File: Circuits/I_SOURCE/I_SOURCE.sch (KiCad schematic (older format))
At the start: 29 parts, among them P1 +8, P2 -8, P3 GND, P4 OUTPUT, P5 I_SELECT, Q1 TIP127, U1 CA3140, U2 LM393

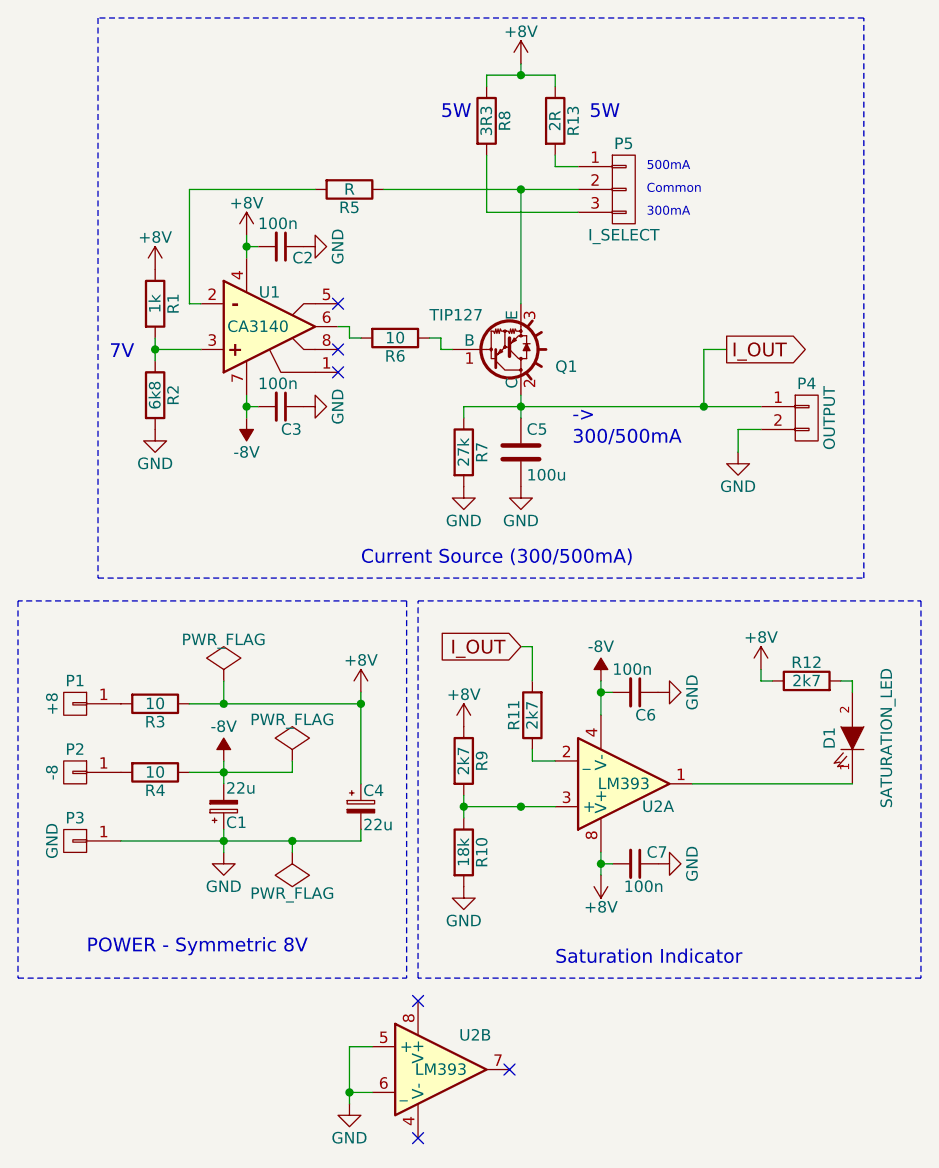
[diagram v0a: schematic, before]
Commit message: ADD: Current Source full PCB design
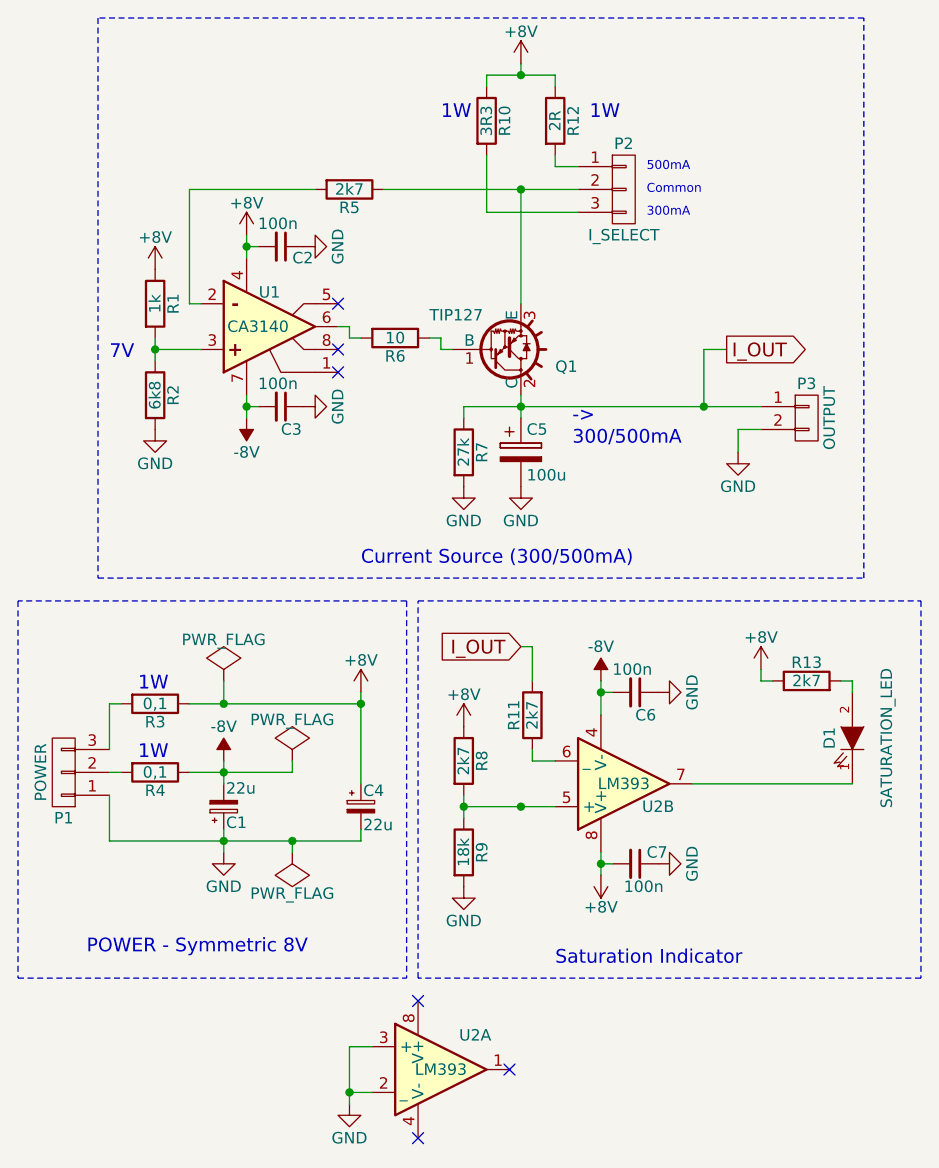
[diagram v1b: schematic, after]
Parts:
- removed C5: 100u, symbol C
- removed P1: +8, symbol CONN_01X01
- removed P2: -8, symbol CONN_01X01
- removed P3: GND, symbol CONN_01X01
- added C5: 100u, Capacitors_THT:CP_Radial_D6.3mm_P2.50mm, symbol CP
- added P1: POWER, Connectors:bornier3, symbol CONN_01X03
- C1, C4, C7: footprint (none) -> Capacitors_THT:CP_Radial_D5.0mm_P2.50mm
- C2, C3, C6: footprint (none) -> Capacitors_THT:C_Rect_L7.0mm_W2.5mm_P5.00mm
- D1: footprint (none) -> LEDs:LED_D5.0mm
- P2: renamed from P5; footprint (none) -> Pin_Headers:Pin_Header_Straight_1x03_Pitch2.00mm
- P3: renamed from P4; footprint (none) -> Connectors:bnc-ci
- Q1: footprint TO-220 -> Power_Integrations:TO-220
- R1, R11, R2, R6, R7: footprint (none) -> w_pth_resistors:RC03
- R10: renamed from R8; footprint (none) -> Resistors_THT:R_Axial_DIN0309_L9.0mm_D3.2mm_P12.70mm_Horizontal
- R12: renamed from R13; footprint (none) -> Resistors_THT:R_Axial_DIN0309_L9.0mm_D3.2mm_P12.70mm_Horizontal
- R13: renamed from R12; footprint (none) -> w_pth_resistors:RC03
- R3, R4: value 10 -> 0,1; footprint (none) -> Resistors_THT:R_Axial_DIN0309_L9.0mm_D3.2mm_P12.70mm_Horizontal
- R5: value R -> 2k7; footprint (none) -> w_pth_resistors:RC03
- R8: renamed from R9; footprint (none) -> w_pth_resistors:RC03
- R9: renamed from R10; footprint (none) -> w_pth_resistors:RC03
- U1, U2: footprint (none) -> Housings_DIP:DIP-8_W7.62mm_LongPads
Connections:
- net GND: now also U2.2 (_), U2.3 (+), C5.2, P1.1 (P1); no longer U2.5 (+), U2.6 (_)
- net I_OUT: now also C5.1
- net at D1.1 (K): now also U2.7; no longer U2.1
- net at R11.1: now also U2.6 (_); no longer U2.2 (_)
- net at R8.2, R9.1: now also U2.5 (+); no longer U2.3 (+)
- net at R3.2: now also P1.3 (P3)
- net at R4.2: now also P1.2 (P2)
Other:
- note added: "1W"
- note removed: "5W"
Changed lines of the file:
@@
 encoding utf-8
 Sheet 1 1
-Title "Current Source for Materials Analysis"
-Date "2017-12-15"
+Title "SADAMAP Current Source "
+Date "2018-01-31"
 Rev "1"
-Comp "LAPMA - UFRGS"
-Comment1 "All resistors are 1/8W, except R8"
+Comp "LAPMA/CTA - IF/UFRGS"
+Comment1 "All resistors are 1/4W, 1% precision, except R3, R4, R8 and R13. "
 Comment2 "300mA and 500mA Selectable DC Current Source"
 Comment3 "There's a saturation indicator for output higher than 7V"
@@
 F 0 "U1" H 1950 2100 50  0000 C CNN
 F 1 "CA3140" H 1900 2250 50  0000 C CNN
-F 2 "" H 1850 2150 50  0000 C CNN
+F 2 "Housings_DIP:DIP-8_W7.62mm_LongPads" H 1850 2150 50  0001 C CNN
 F 3 "" H 1950 2250 50  0000 C CNN
 	1    1950 2250
@@
 P 2300 1650
 F 0 "R5" V 2380 1650 50  0000 C CNN
-F 1 "R" V 2300 1650 50  0000 C CNN
-F 2 "" V 2230 1650 50  0000 C CNN
+F 1 "2k7" V 2300 1650 50  0000 C CNN
+F 2 "w_pth_resistors:RC03" V 2230 1650 50  0001 C CNN
 F 3 "" H 2300 1650 50  0000 C CNN
 	1    2300 1650
@@
 	1600 2150 1650 2150
 $Comp
-L R R8
+L R R10
 U 1 1 5A2F411C
 P 2900 1350
-F 0 "R8" V 2980 1350 50  0000 C CNN
+F 0 "R10" V 2980 1350 50  0000 C CNN
 F 1 "3R3" V 2900 1350 50  0000 C CNN
-F 2 "" V 2830 1350 50  0000 C CNN
+F 2 "Resistors_THT:R_Axial_DIN0309_L9.0mm_D3.2mm_P12.70mm_Horizontal" V 2830 1350 50  0001 C CNN
 F 3 "" H 2900 1350 50  0000 C CNN
 	1    2900 1350
@@
 F 0 "Q1" H 3200 2425 50  0000 L CNN
 F 1 "TIP127" H 2650 2200 50  0000 L CNN
-F 2 "TO-220" H 2600 2250 50  0001 L CIN
+F 2 "Power_Integrations:TO-220" H 2600 2250 50  0001 L CIN
 F 3 "" H 2950 2350 50  0000 L CNN
 	1    2950 2350
@@
 F 0 "R6" V 2580 2300 50  0000 C CNN
 F 1 "10" V 2500 2300 50  0000 C CNN
-F 2 "" V 2430 2300 50  0000 C CNN
+F 2 "w_pth_resistors:RC03" V 2430 2300 50  0001 C CNN
 F 3 "" H 2500 2300 50  0000 C CNN
 	1    2500 2300
@@
 F 0 "R7" V 2880 2800 50  0000 C CNN
 F 1 "27k" V 2800 2800 50  0000 C CNN
-F 2 "" V 2730 2800 50  0000 C CNN
+F 2 "w_pth_resistors:RC03" V 2730 2800 50  0001 C CNN
 F 3 "" H 2800 2800 50  0000 C CNN
 	1    2800 2800
-	1    0    0    -1
-$EndComp
-$Comp
-L C C5
-U 1 1 5A2F43CF
-P 3050 2800
-F 0 "C5" H 3075 2900 50  0000 L CNN
-F 1 "100u" H 3075 2700 50  0000 L CNN
-F 2 "" H 3088 2650 50  0000 C CNN
-F 3 "" H 3050 2800 50  0000 C CNN
-	1    3050 2800
 	1    0    0    -1
 $EndComp
@@
 $Comp
 L LM393 U2
-U 1 1 5A2F4B6B
+U 2 1 5A2F4B6B
 P 3500 4250
 F 0 "U2" H 3650 4350 50  0000 C CNN
 F 1 "LM393" H 3500 4250 50  0000 C CNN
-F 2 "" H 3500 4250 50  0000 C CNN
+F 2 "Housings_DIP:DIP-8_W7.62mm_LongPads" H 3500 4250 50  0001 C CNN
 F 3 "" H 3500 4250 50  0000 C CNN
-	1    3500 4250
+	2    3500 4250
 	1    0    0    1
 $EndComp
 $Comp
 L LM393 U2
-U 2 1 5A2F4B6C
+U 1 1 5A2F4B6C
 P 2700 5500
 F 0 "U2" H 2850 5650 50  0000 C CNN
 F 1 "LM393" H 2700 5500 50  0000 C CNN
-F 2 "" H 2700 5500 50  0000 C CNN
+F 2 "Housings_DIP:DIP-8_W7.62mm_LongPads" H 2700 5500 50  0001 C CNN
 F 3 "" H 2700 5500 50  0000 C CNN
-	2    2700 5500
+	1    2700 5500
 	1    0    0    -1
 $EndComp
@@
 F 0 "R11" V 3180 3950 50  0000 C CNN
 F 1 "2k7" V 3100 3950 50  0000 C CNN
-F 2 "" V 3030 3950 50  0000 C CNN
+F 2 "w_pth_resistors:RC03" V 3030 3950 50  0001 C CNN
 F 3 "" H 3100 3950 50  0000 C CNN
 	1    3100 3950
@@
 F 0 "C6" V 3650 3850 50  0000 L CNN
 F 1 "100n" V 3450 3750 50  0000 L CNN
-F 2 "" H 3550 3850 50  0000 C CNN
+F 2 "Capacitors_THT:C_Rect_L7.0mm_W2.5mm_P5.00mm" H 3550 3850 50  0001 C CNN
 F 3 "" H 3550 3850 50  0000 C CNN
 	1    3550 3850
@@
 $EndComp
 $Comp
-L R R9
+L R R8
 U 1 1 5A2F4B71
 P 2800 4150
-F 0 "R9" V 2880 4150 50  0000 C CNN
+F 0 "R8" V 2880 4150 50  0000 C CNN
 F 1 "2k7" V 2800 4150 50  0000 C CNN
-F 2 "" V 2730 4150 50  0000 C CNN
+F 2 "w_pth_resistors:RC03" V 2730 4150 50  0001 C CNN
 F 3 "" H 2800 4150 50  0000 C CNN
 	1    2800 4150
@@
 $EndComp
 $Comp
-L R R10
+L R R9
 U 1 1 5A2F4B72
 P 2800 4550
-F 0 "R10" V 2880 4550 50  0000 C CNN
+F 0 "R9" V 2880 4550 50  0000 C CNN
 F 1 "18k" V 2800 4550 50  0000 C CNN
-F 2 "" V 2730 4550 50  0000 C CNN
+F 2 "w_pth_resistors:RC03" V 2730 4550 50  0001 C CNN
 F 3 "" H 2800 4550 50  0000 C CNN
 	1    2800 4550
@@
 F 0 "C7" V 3600 4650 50  0000 L CNN
 F 1 "100n" V 3450 4550 50  0000 L CNN
-F 2 "" H 3550 4600 50  0000 C CNN
+F 2 "Capacitors_THT:CP_Radial_D5.0mm_P2.50mm" H 3550 4600 50  0001 C CNN
 F 3 "" H 3550 4600 50  0000 C CNN
 	1    3550 4600
@@
 F 0 "D1" H 4500 3950 50  0000 C CNN
 F 1 "SATURATION_LED" H 4500 4200 50  0000 C CNN
-F 2 "" H 4500 4050 50  0000 C CNN
+F 2 "LEDs:LED_D5.0mm" H 4500 4050 50  0001 C CNN
 F 3 "" H 4500 4050 50  0000 C CNN
 	1    4500 4050
@@
 $EndComp
 $Comp
-L R R12
+L R R13
 U 1 1 5A2F4B7B
 P 4300 3800
-F 0 "R12" V 4380 3800 50  0000 C CNN
+F 0 "R13" V 4380 3800 50  0000 C CNN
 F 1 "2k7" V 4300 3800 50  0000 C CNN
-F 2 "" V 4230 3800 50  0000 C CNN
+F 2 "w_pth_resistors:RC03" V 4230 3800 50  0001 C CNN
 F 3 "" H 4300 3800 50  0000 C CNN
 	1    4300 3800
@@
 NoConn ~ 3000 5500
 $Comp
-L CONN_01X01 P1
-U 1 1 5A2F4B7E
-P 1100 3900
-F 0 "P1" H 1100 4000 50  0000 C CNN
-F 1 "+8" V 1200 3900 50  0000 C CNN
-F 2 "" H 1100 3900 50  0000 C CNN
-F 3 "" H 1100 3900 50  0000 C CNN
-	1    1100 3900
-	-1   0    0    -1
-$EndComp
-$Comp
-L CONN_01X01 P2
-U 1 1 5A2F4B7F
-P 1100 4200
-F 0 "P2" H 1100 4300 50  0000 C CNN
-F 1 "-8" V 1200 4200 50  0000 C CNN
-F 2 "" H 1100 4200 50  0000 C CNN
-F 3 "" H 1100 4200 50  0000 C CNN
-	1    1100 4200
-	-1   0    0    -1
-$EndComp
-$Comp
-L CONN_01X01 P3
-U 1 1 5A2F4B80
-P 1100 4500
-F 0 "P3" H 1100 4600 50  0000 C CNN
-F 1 "GND" V 1200 4500 50  0000 C CNN
-F 2 "" H 1100 4500 50  0000 C CNN
-F 3 "" H 1100 4500 50  0000 C CNN
-	1    1100 4500
-	-1   0    0    -1
-$EndComp
-$Comp
 L R R3
 U 1 1 5A2F4B81
 P 1450 3900
 F 0 "R3" V 1530 3900 50  0000 C CNN
-F 1 "10" V 1450 3900 50  0000 C CNN
-F 2 "" V 1380 3900 50  0000 C CNN
+F 1 "0,1" V 1450 3900 50  0000 C CNN
+F 2 "Resistors_THT:R_Axial_DIN0309_L9.0mm_D3.2mm_P12.70mm_Horizontal" V 1380 3900 50  0001 C CNN
 F 3 "" H 1450 3900 50  0000 C CNN
 	1    1450 3900
@@
 P 1450 4200
 F 0 "R4" V 1530 4200 50  0000 C CNN
-F 1 "10" V 1450 4200 50  0000 C CNN
-F 2 "" V 1380 4200 50  0000 C CNN
+F 1 "0,1" V 1450 4200 50  0000 C CNN
+F 2 "Resistors_THT:R_Axial_DIN0309_L9.0mm_D3.2mm_P12.70mm_Horizontal" V 1380 4200 50  0001 C CNN
 F 3 "" H 1450 4200 50  0000 C CNN
 	1    1450 4200
@@
 F 0 "C1" H 1760 4420 50  0000 L CNN
 F 1 "22u" H 1760 4270 50  0000 L CNN
-F 2 "" H 1750 4350 50  0000 C CNN
+F 2 "Capacitors_THT:CP_Radial_D5.0mm_P2.50mm" H 1750 4350 50  0001 C CNN
 F 3 "" H 1750 4350 50  0000 C CNN
 	1    1750 4350
@@
 F 0 "C4" H 2360 4420 50  0000 L CNN
 F 1 "22u" H 2360 4270 50  0000 L CNN
-F 2 "" H 2350 4350 50  0000 C CNN
+F 2 "Capacitors_THT:CP_Radial_D5.0mm_P2.50mm" H 2350 4350 50  0001 C CNN
 F 3 "" H 2350 4350 50  0000 C CNN
 	1    2350 4350
@@
 	1750 4450 1750 4550
 Wire Wire Line
-	1300 4500 2350 4500
+	1250 4500 2350 4500
 Wire Wire Line
 	2350 4500 2350 4450
@@
 F 0 "R1" V 1530 2150 50  0000 C CNN
 F 1 "1k" V 1450 2150 50  0000 C CNN
-F 2 "" V 1380 2150 50  0000 C CNN
+F 2 "w_pth_resistors:RC03" V 1380 2150 50  0001 C CNN
 F 3 "" H 1450 2150 50  0000 C CNN
 	1    1450 2150
@@
 F 0 "R2" V 1530 2550 50  0000 C CNN
 F 1 "6k8" V 1450 2550 50  0000 C CNN
-F 2 "" V 1380 2550 50  0000 C CNN
+F 2 "w_pth_resistors:RC03" V 1380 2550 50  0001 C CNN
 F 3 "" H 1450 2550 50  0000 C CNN
 	1    1450 2550
@@
 F 0 "C3" V 2100 2600 50  0000 L CNN
 F 1 "100n" V 1900 2500 50  0000 L CNN
-F 2 "" H 2000 2600 50  0000 C CNN
+F 2 "Capacitors_THT:C_Rect_L7.0mm_W2.5mm_P5.00mm" H 2000 2600 50  0001 C CNN
 F 3 "" H 2000 2600 50  0000 C CNN
 	1    2000 2600
@@
 F 0 "C2" V 2050 1950 50  0000 L CNN
 F 1 "100n" V 1900 1800 50  0000 L CNN
-F 2 "" H 2000 1900 50  0000 C CNN
+F 2 "Capacitors_THT:C_Rect_L7.0mm_W2.5mm_P5.00mm" H 2000 1900 50  0001 C CNN
 F 3 "" H 2000 1900 50  0000 C CNN
 	1    2000 1900
@@
 	2800 2600 4100 2600
 $Comp
-L CONN_01X02 P4
+L CONN_01X02 P3
 U 1 1 5A2F6EE0
 P 4300 2650
-F 0 "P4" H 4300 2800 50  0000 C CNN
+F 0 "P3" H 4300 2800 50  0000 C CNN
 F 1 "OUTPUT" V 4400 2650 50  0000 C CNN
-F 2 "" H 4300 2650 50  0000 C CNN
+F 2 "Connectors:bnc-ci" H 4300 2650 50  0001 C CNN
 F 3 "" H 4300 2650 50  0000 C CNN
 	1    4300 2650
@@
 7V
 Text Notes 2700 1350 0    60   ~ 0
-5W
+1W
 Text Notes 2350 3300 0    60   ~ 0
 Current Source (300/500mA)
@@
 	2600 3450 4800 3450
 $Comp
-L R R13
+L R R12
 U 1 1 5A4CC621
 P 3200 1350
-F 0 "R13" V 3280 1350 50  0000 C CNN
+F 0 "R12" V 3280 1350 50  0000 C CNN
 F 1 "2R" V 3200 1350 50  0000 C CNN
-F 2 "" V 3130 1350 50  0000 C CNN
+F 2 "Resistors_THT:R_Axial_DIN0309_L9.0mm_D3.2mm_P12.70mm_Horizontal" V 3130 1350 50  0001 C CNN
 F 3 "" H 3200 1350 50  0000 C CNN
 	1    3200 1350
@@
 $EndComp
 Text Notes 3350 1350 0    60   ~ 0
-5W
+1W
 Wire Wire Line
 	2900 1200 2900 1150
@@
 Connection ~ 3050 1150
 $Comp
-L CONN_01X03 P5
+L CONN_01X03 P2
 U 1 1 5A4CD4EF
 P 3500 1650
-F 0 "P5" H 3500 1850 50  0000 C CNN
+F 0 "P2" H 3500 1850 50  0000 C CNN
 F 1 "I_SELECT" H 3500 1450 50  0000 C CNN
-F 2 "" H 3500 1650 50  0000 C CNN
+F 2 "Pin_Headers:Pin_Header_Straight_1x03_Pitch2.00mm" H 3500 1650 50  0001 C CNN
 F 3 "" H 3500 1650 50  0000 C CNN
 	1    3500 1650
@@
 Text Notes 3600 1675 0    39   ~ 0
 Common
+Text Notes 1375 3850 0    60   ~ 0
+1W
+Text Notes 1375 4150 0    60   ~ 0
+1W
+$Comp
+L CP C5
+U 1 1 5A724097
+P 3050 2800
+F 0 "C5" H 3075 2900 50  0000 L CNN
+F 1 "100u" H 3075 2700 50  0000 L CNN
+F 2 "Capacitors_THT:CP_Radial_D6.3mm_P2.50mm" H 3088 2650 50  0001 C CNN
+F 3 "" H 3050 2800 50  0000 C CNN
+	1    3050 2800
+	1    0    0    -1
+$EndComp
+$Comp
+L CONN_01X03 P1
+U 1 1 5A7244BA
+P 1050 4200
+F 0 "P1" H 1050 4400 50  0000 C CNN
+F 1 "POWER" V 1150 4200 50  0000 C CNN
+F 2 "Connectors:bornier3" H 1050 4200 50  0001 C CNN
+F 3 "" H 1050 4200 50  0000 C CNN
+	1    1050 4200
+	-1   0    0    1
+$EndComp
+Wire Wire Line
+	1250 4200 1300 4200
+Wire Wire Line
+	1250 4100 1250 3900
+Wire Wire Line
+	1250 3900 1300 3900
+Wire Wire Line
+	1250 4300 1250 4500
 $EndSCHEMATC

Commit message: EDIT: REORGANIZING FILES
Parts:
- C1, C4: symbol CP_Small -> I_SOURCE-rescue:CP_Small
- C2, C3, C6, C7: symbol C_Small -> I_SOURCE-rescue:C_Small
- C5: symbol CP -> I_SOURCE-rescue:CP
- D1: symbol LED -> I_SOURCE-rescue:LED
- P1, P2: symbol CONN_01X03 -> I_SOURCE-rescue:CONN_01X03
- P3: symbol CONN_01X02 -> I_SOURCE-rescue:CONN_01X02
- Q1: symbol TIP126 -> I_SOURCE-rescue:TIP126
- R1, R10, R11, R12, R13, R2, R3, R4, R5, R6, R7, R8, R9: symbol R -> I_SOURCE-rescue:R
- U1: symbol CA3140 -> I_SOURCE-rescue:CA3140
- U2: symbol LM393 -> I_SOURCE-rescue:LM393
